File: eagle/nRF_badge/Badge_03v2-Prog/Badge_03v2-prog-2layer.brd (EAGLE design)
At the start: 72.4 x 61 mm, 4 parts, among them J1 PROG_CONN_6

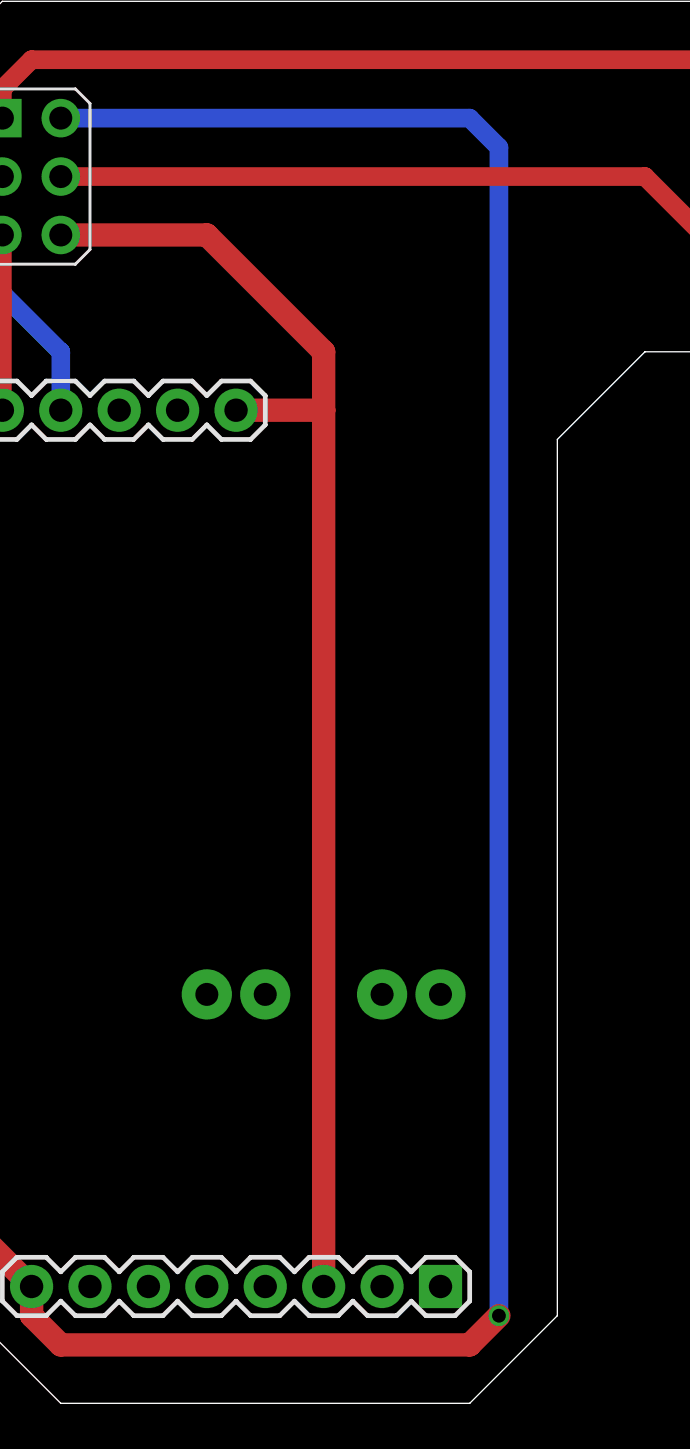
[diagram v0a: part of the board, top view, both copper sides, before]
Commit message: Added power LED to programmer. Gerber files
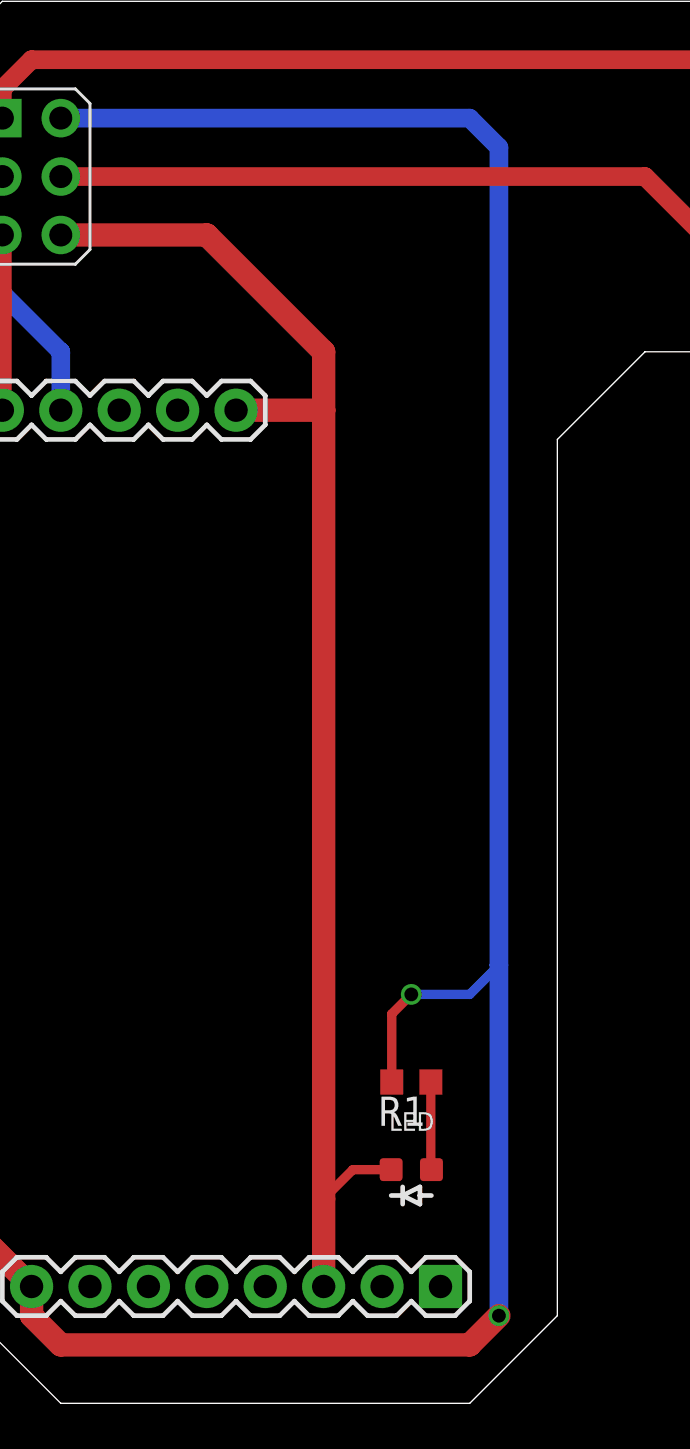
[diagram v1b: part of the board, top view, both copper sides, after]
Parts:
- added LED: (no value), Badge:LED-0603
- added R1: (no value), rcl:R0603
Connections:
- new net N$1: LED.A, R1.1
- net GND: now also LED.C
- net VCC: now also R1.2
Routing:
- net VCC: track 132.7 -> 141.2 mm, vias 1 -> 2
- net N$1: track 0.00 -> 3.82 mm
- net GND: track 58.0 -> 61.4 mm
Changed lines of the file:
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@@
 <?xml version="1.0" encoding="utf-8"?>
 <!DOCTYPE eagle SYSTEM "eagle.dtd">
-<eagle version="7.4.0">
+<eagle version="7.7.0">
 <drawing>
 <settings>
@@
 <element name="UART" library="Badge" package="1X08_ROUND" value="8HEADERM" x="52.07" y="53.34" smashed="yes"/>
 <element name="PROG" library="Badge" package="1X08_ROUND" value="8HEADERM" x="2.54" y="43.18" smashed="yes"/>
+<element name="LED" library="Badge" package="LED-0603" value="" x="27.94" y="10.16"/>
+<element name="R1" library="rcl" package="R0603" value="" x="27.94" y="13.97" rot="R180"/>
 </elements>
 <signals>
@@
 <contactref element="POWER" pad="3"/>
 <wire x1="20.32" y1="43.18" x2="24.13" y2="43.18" width="1.016" layer="1"/>
-<wire x1="24.13" y1="43.18" x2="24.13" y2="5.08" width="1.016" layer="1"/>
+<wire x1="24.13" y1="43.18" x2="24.13" y2="8.89" width="1.016" layer="1"/>
+<wire x1="24.13" y1="8.89" x2="24.13" y2="5.08" width="1.016" layer="1"/>
 <wire x1="12.7" y1="50.8" x2="19.05" y2="50.8" width="1.016" layer="1"/>
 <wire x1="19.05" y1="50.8" x2="24.13" y2="45.72" width="1.016" layer="1"/>
 <wire x1="24.13" y1="45.72" x2="24.13" y2="43.18" width="1.016" layer="1"/>
+<contactref element="LED" pad="C"/>
+<wire x1="27.063" y1="10.16" x2="25.4" y2="10.16" width="0.4064" layer="1"/>
+<wire x1="25.4" y1="10.16" x2="24.13" y2="8.89" width="0.4064" layer="1"/>
 </signal>
 <signal name="VCC">
@@
 <wire x1="12.7" y1="55.88" x2="30.48" y2="55.88" width="0.8128" layer="16"/>
 <wire x1="30.48" y1="55.88" x2="31.75" y2="54.61" width="0.8128" layer="16"/>
-<wire x1="31.75" y1="54.61" x2="31.75" y2="3.81" width="0.8128" layer="16"/>
+<wire x1="31.75" y1="54.61" x2="31.75" y2="19.05" width="0.8128" layer="16"/>
 <via x="31.75" y="3.81" extent="1-16" drill="0.6"/>
+<contactref element="R1" pad="2"/>
+<wire x1="31.75" y1="19.05" x2="31.75" y2="3.81" width="0.8128" layer="16"/>
+<wire x1="27.09" y1="13.97" x2="27.09" y2="16.93" width="0.4064" layer="1"/>
+<wire x1="27.09" y1="16.93" x2="27.94" y2="17.78" width="0.4064" layer="1"/>
+<via x="27.94" y="17.78" extent="1-16" drill="0.6"/>
+<wire x1="27.94" y1="17.78" x2="30.48" y2="17.78" width="0.4064" layer="16"/>
+<wire x1="30.48" y1="17.78" x2="31.75" y2="19.05" width="0.4064" layer="16"/>
 </signal>
 <signal name="SWDIO">
@@
 <wire x1="7.62" y1="53.34" x2="10.16" y2="53.34" width="0.8128" layer="16"/>
 </signal>
-<signal name="N$3">
-<via x="29.21" y="17.78" extent="1-16" drill="1" diameter="2.1844"/>
-</signal>
-<signal name="N$4">
-<via x="26.67" y="17.78" extent="1-16" drill="1" diameter="2.1844"/>
-</signal>
-<signal name="N$6">
-<via x="21.59" y="17.78" extent="1-16" drill="1" diameter="2.1844"/>
-</signal>
-<signal name="N$7">
-<via x="19.05" y="17.78" extent="1-16" drill="1" diameter="2.1844"/>
+<signal name="N$1">
+<contactref element="R1" pad="1"/>
+<contactref element="LED" pad="A"/>
+<wire x1="28.79" y1="13.97" x2="28.79" y2="10.187" width="0.4064" layer="1"/>
+<wire x1="28.79" y1="10.187" x2="28.817" y2="10.16" width="0.4064" layer="1"/>
 </signal>
 </signals>
